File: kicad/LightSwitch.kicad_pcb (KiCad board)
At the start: 2 copper layers, 42 x 70 mm, 26 parts, among them J2 RJ45, J3 RJ45, SW1 Pushbutton_LED, SW2 Pushbutton_LED, SW3 Pushbutton_LED, SW4 Pushbutton_LED, SW5 Pushbutton_LED, SW6 Pushbutton_LED, U1 LM1117-5.0, U2 ATtiny406-M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

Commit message: Parking stuff, so I can contemplate the use of a nrf52840 _with_ DALI
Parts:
- removed J3: RJ45, Connector_RJ:RJ45_Amphenol_54602-x08_Horizontal
- removed PROG: Conn_01x03_Male, Connector_PinHeader_2.54mm:PinHeader_1x03_P2.54mm_Vertical
- removed R3, R8: 220, Resistor_SMD:R_0805_2012Metric
- removed REF** (x4): MountingHole_3mm_Pad, MountingHole:MountingHole_3mm_Pad
- removed SW6: Pushbutton_LED, LightSwitch:12x12x7.3 LED Pushbutton
- removed TERM: Jumper, Connector_PinHeader_2.54mm:PinHeader_1x02_P2.54mm_Vertical
- added C3: 10u, Capacitor_SMD:C_0805_2012Metric, F.Cu at (118.4, 74.6)
- added C4: 0.1u, Capacitor_SMD:C_0805_2012Metric, F.Cu at (121.0, 145.2)
- added C5: 0.1u, Capacitor_SMD:C_0805_2012Metric, F.Cu at (116.2, 99.8)
- added D1: 1N4148WS, Diode_SMD:D_SOD-323, F.Cu at (119.3, 67.5)
- added D2: D_Bridge_+-AA, imported_modules:SOIC245P670X290-4N, F.Cu at (121.1, 43.6)
- added D3: 1N4148WS, Diode_SMD:D_SOD-323, F.Cu at (124.2, 52.3)
- added D4: 1N4148WS, Diode_SMD:D_SOD-323, F.Cu at (127.6, 52.3)
- added J1: Screw_Terminal_01x02, TerminalBlock_Phoenix:TerminalBlock_Phoenix_MKDS-1,5-2-5.08_1x02_P5.08mm_Horizontal, B.Cu at (118.5, 25.4)
- added Q1: MMBT2222A, Package_TO_SOT_SMD:SOT-23, F.Cu at (116.5, 51.5)
- added R1: 4.7K, Resistor_SMD:R_0805_2012Metric, F.Cu at (128.2, 97.0)
- C1: value 0.1u -> 10u
- C2: value 10u -> 0.1u
- J2: value RJ45 -> Conn_01x03_Male; footprint Connector_RJ:RJ45_Amphenol_54602-x08_Horizontal -> Connector_PinHeader_2.54mm:PinHeader_1x03_P2.54mm_Vertical; moved to F.Cu
- R2: value 220 -> 4.7K
- R4: value 220 -> 120
- R5: value 120 -> 1K
- R6: value 220 -> 27K
- R7: value 220 -> 2K
- SW1, SW2, SW3, SW4, SW5: value Pushbutton_LED -> SW_Push; footprint LightSwitch:12x12x7.3 LED Pushbutton -> Button_Switch_THT:SW_PUSH-12mm
- U1: value LM1117-5.0 -> LM2936-3.3; footprint Package_TO_SOT_SMD:SOT-223-3_TabPin2 -> Package_TO_SOT_SMD:SOT-223
- U2: value ATtiny406-M -> SHT35-DIS; footprint Package_DFN_QFN:VQFN-20-1EP_3x3mm_P0.4mm_EP1.7x1.7mm -> Sensor_Humidity:Sensirion_DFN-8-1EP_2.5x2.5mm_P0.5mm_EP1.1x1.7mm
- U3: value SN65HVD232 -> ATtiny804-SS; footprint Package_SO:SOIC-8_3.9x4.9mm_P1.27mm -> Package_SO:SOIC-14_3.9x8.7mm_P1.27mm
- moved R6 108.0 mm to (124.1, 50.2), turned to 0 degrees
- moved R5 100.2 mm to (113.5, 51.5), turned to -90 degrees
- moved R7 99.4 mm to (127.7, 50.2)
- moved SW2 99.1 mm to (115.0, 57.0)
- moved SW4 97.8 mm to (115.0, 107.0)
- moved C1 97.1 mm to (117.2, 71.0)
- moved C2 93.7 mm to (119.3, 71.0), turned to -90 degrees
- moved R4 91.4 mm to (114.5, 48.7), turned to 180 degrees
- moved U2 90.6 mm to (121.0, 142.5), turned to -90 degrees
- moved SW1 84.3 mm to (115.0, 32.0)
- moved U1 83.5 mm to (124.8, 72.2)
- moved J2 81.2 mm to (112.1, 93.6), turned to 90 degrees
- moved U3 79.3 mm to (121.9, 99.5), turned to 90 degrees
- moved SW3 74.5 mm to (115.2, 82.0)
- moved SW5 72.8 mm to (115.0, 132.0)
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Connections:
- C1 pad 1: VDD -> Net-(C1-Pad1)
- C2 pad 1: VDD -> Net-(C1-Pad1)
- J2 pad 1: /CANH -> VDD
- J2 pad 2: /CANL -> /PROG
- R2 pad 1: /LED1 -> VDD
- R2 pad 2: Net-(R2-Pad2) -> /SCL
- R4 pad 1: /LED3 -> Net-(Q1-Pad1)
- R4 pad 2: Net-(R4-Pad2) -> /DALI_TX
- R5 pad 1: Net-(JP1-Pad2) -> /DALI_TX
- R5 pad 2: /CANL -> GND
- R6 pad 1: /LED4 -> /DALI+
- R6 pad 2: Net-(R6-Pad2) -> /DALI_RX
- R7 pad 1: /LED5 -> /DALI_RX
- R7 pad 2: Net-(R7-Pad2) -> GND
- SW1 pad 1: GND -> /SW1
- SW1 pad 2: Net-(SW1-Pad2) -> GND
- SW2 pad 1: GND -> /SW2
- SW2 pad 2: Net-(SW2-Pad2) -> GND
- SW3 pad 1: GND -> /SW3
- SW3 pad 2: Net-(SW3-Pad2) -> GND
- SW4 pad 1: GND -> /SW4
- SW4 pad 2: Net-(SW4-Pad2) -> GND
- SW5 pad 1: GND -> /SW5
- SW5 pad 2: Net-(SW5-Pad2) -> GND
- U1 pad 1: GND -> Net-(C1-Pad1)
- U1 pad 2: VDD -> GND
- U1 pad 3: /VIN -> VDD
- U2 pad 1: Net-(U2-Pad1) -> /SDA
- U2 pad 2: Net-(U2-Pad2) -> GND
- U2 pad 3: GND -> /TEMP_ALERT
- U2 pad 4: VDD -> /SCL
- U2 pad 5: /LED3 -> VDD
- U2 pad 6: /SW3 -> unconnected-(U2-Pad6)
- U2 pad 7: /LED5 -> GND
- U2 pad 8: /SW5 -> GND
- U2 pad 9: /LED6 -> GND
- U3 pad 1: /CAN_TX -> VDD
- U3 pad 2: GND -> /SW4
- U3 pad 3: VDD -> /SW5
- U3 pad 4: /CAN_RX -> /DALI_TX
- U3 pad 5: Net-(U3-Pad5) -> /DALI_RX
- U3 pad 6: /CANL -> /TEMP_ALERT
- U3 pad 7: /CANH -> /SCL
- U3 pad 8: Net-(U3-Pad8) -> /SDA
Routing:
- net VDD: track 40.3 -> 129.6 mm
- net /DALI_TX: track 0.00 -> 68.0 mm
- net /DALI_RX: track 0.00 -> 62.4 mm
- net /SDA: track 0.00 -> 54.8 mm
- net /LED1: track 54.3 -> 0.00 mm
- net /CANL: track 50.8 -> 0.00 mm, vias 1 -> 0
- net /TEMP_ALERT: track 0.00 -> 48.3 mm
- net /SW1: track 43.9 -> 87.5 mm
- net GND: track 18.0 -> 61.2 mm, vias 6 -> 0
- net /SCL: track 0.00 -> 43.1 mm
- net /VIN: track 37.0 -> 0.00 mm
- net Net-(J2-Pad7): track 36.3 -> 0.00 mm
- net /CANH: track 35.6 -> 0.00 mm
- net /LED2: track 34.6 -> 0.00 mm
- net /LED5: track 31.7 -> 0.00 mm
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- added copper zone on F.Cu, net GND
- removed copper zone on B.Cu, net GND
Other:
- board size 42 x 70 mm -> 42 x 129.3 mm
- net class Default removed
- board text added: "GND"
- board text added: "PRG"
- board text added: "VDD"

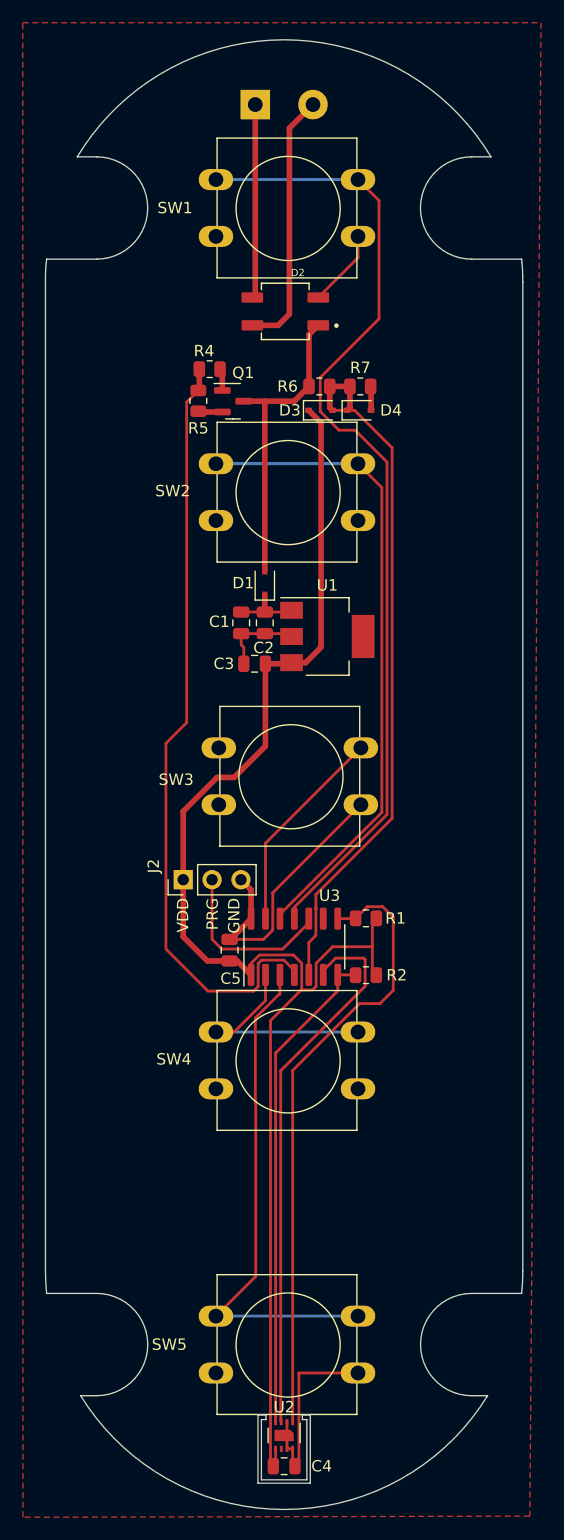
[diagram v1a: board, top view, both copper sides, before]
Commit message: Updated with NRF52840 version. Modded since sending to OSHPark
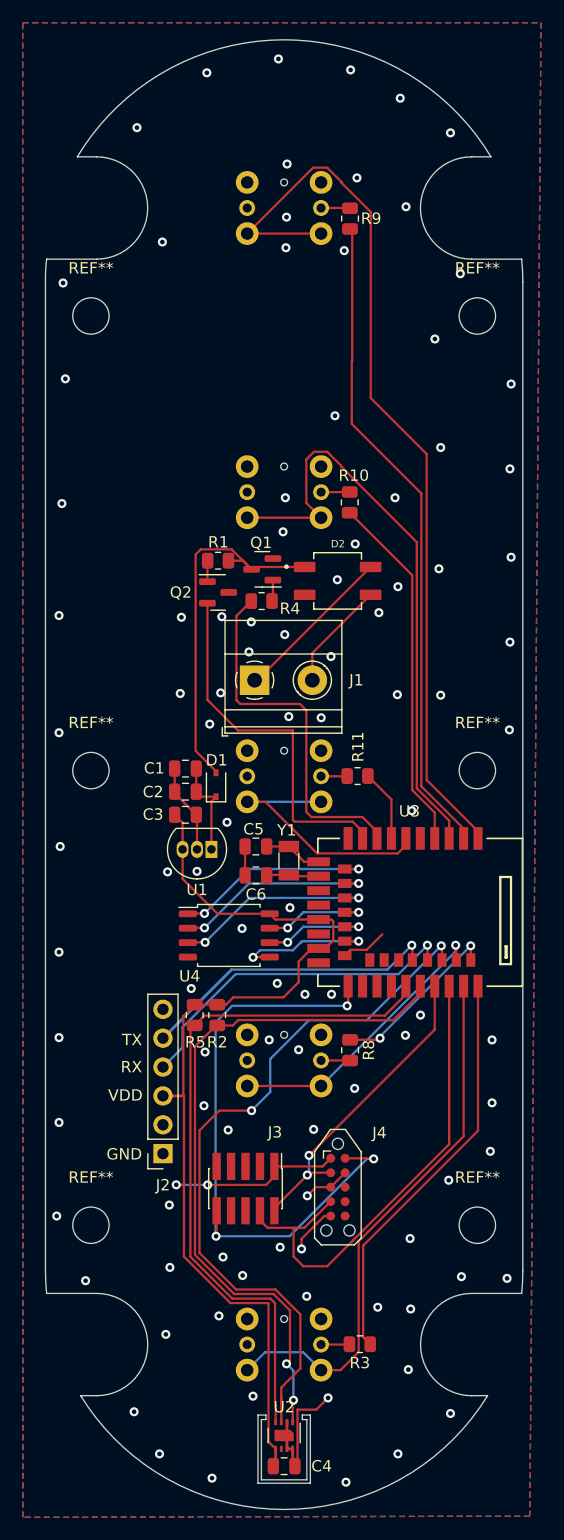
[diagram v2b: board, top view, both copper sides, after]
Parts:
- removed D3, D4: 1N4148WS, Diode_SMD:D_SOD-323
- removed R6: 27K, Resistor_SMD:R_0805_2012Metric
- removed R7: 2K, Resistor_SMD:R_0805_2012Metric
- added C6: 12pf, Capacitor_SMD:C_0805_2012Metric, F.Cu at (118.5, 93.2)
- added J3: Conn_ARM_JTAG_SWD_10, Connector_PinHeader_1.27mm:PinHeader_2x05_P1.27mm_Vertical_SMD, F.Cu at (117.6, 120.8)
- added J4: Conn_ARM_JTAG_SWD_10, Connector:Tag-Connect_TC2050-IDC-NL_2x05_P1.27mm_Vertical, F.Cu at (125.7, 120.7)
- added Q2: MMBT2222A, Package_TO_SOT_SMD:SOT-23, F.Cu at (115.2, 68.3)
- added R10: 330, Resistor_SMD:R_0805_2012Metric, F.Cu at (126.8, 60.4)
- added R11: 330, Resistor_SMD:R_0805_2012Metric, F.Cu at (127.5, 84.5)
- added R3: 330, Resistor_SMD:R_0805_2012Metric, F.Cu at (127.7, 134.5)
- added R8: 330, Resistor_SMD:R_0805_2012Metric, F.Cu at (126.8, 108.6)
- added R9: 330, Resistor_SMD:R_0805_2012Metric, F.Cu at (126.8, 35.4)
- added REF**: MountingHole_3.2mm_M3, MountingHole:MountingHole_3.2mm_M3, F.Cu at (104.0, 84.0)
- added REF**: MountingHole_3.2mm_M3, MountingHole:MountingHole_3.2mm_M3, F.Cu at (138.0, 84.0)
- added REF**: MountingHole_3.2mm_M3, MountingHole:MountingHole_3.2mm_M3, F.Cu at (104.0, 44.0)
- added REF**: MountingHole_3.2mm_M3, MountingHole:MountingHole_3.2mm_M3, F.Cu at (104.0, 124.0)
- added REF**: MountingHole_3.2mm_M3, MountingHole:MountingHole_3.2mm_M3, F.Cu at (138.0, 44.0)
- added REF**: MountingHole_3.2mm_M3, MountingHole:MountingHole_3.2mm_M3, F.Cu at (138.0, 124.0)
- added U4: MX25R3235FM2xx0, Package_SO:SOP-8_5.28x5.23mm_P1.27mm, F.Cu at (116.1, 98.5)
- added Y1: 32.768kHz, Crystal:Crystal_SMD_3215-2Pin_3.2x1.5mm, F.Cu at (121.4, 91.9)
- C5: value 0.1u -> 12pf
- J1: moved to F.Cu
- J2: value Conn_01x03_Male -> Conn_01x06_Female; footprint Connector_PinHeader_2.54mm:PinHeader_1x03_P2.54mm_Vertical -> Connector_PinSocket_2.54mm:PinSocket_1x06_P2.54mm_Vertical
- R1: value 4.7K -> 2.2K
- R2: value 4.7K -> 10K
- R5: value 1K -> 10K
- SW1, SW2, SW3, SW4, SW5: value SW_Push -> SW_Push_LED; footprint Button_Switch_THT:SW_PUSH-12mm -> LocalProject:LED Pushbutton; moved to B.Cu
- U1: value LM2936-3.3 -> LM2936-3.0; footprint Package_TO_SOT_SMD:SOT-223 -> Package_TO_SOT_THT:TO-92_Inline
- U3: value ATtiny804-SS -> E73-2G4M08S1C; footprint Package_SO:SOIC-14_3.9x8.7mm_P1.27mm -> E73-2G4M08S1C:E73-2G4M08S1C
- moved R5 54.0 mm to (113.1, 105.5)
- moved J1 50.6 mm to (118.4, 76.0)
- moved R1 34.1 mm to (115.2, 65.5)
- moved J2 24.2 mm to (110.3, 117.7), turned to 180 degrees
- moved D2 24.2 mm to (125.7, 67.3), turned to 0 degrees
- moved U1 21.3 mm to (114.6, 90.9), turned to 180 degrees
- moved R4 20.9 mm to (119.0, 69.1)
- moved D1 18.3 mm to (115.0, 85.2)
- moved C2 16.4 mm to (112.3, 85.9), turned to 180 degrees
- moved Q1 15.0 mm to (119.1, 66.3), turned to 180 degrees
- moved C3 14.6 mm to (112.3, 87.9), turned to 0 degrees
- moved C1 13.7 mm to (112.3, 83.8), turned to 180 degrees
- moved R2 13.6 mm to (115.1, 105.5), turned to -90 degrees
- moved U3 9.63 mm to (131.0, 96.5)
- moved C5 9.41 mm to (118.5, 90.7), turned to 180 degrees
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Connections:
- C5 pad 1: GND -> Net-(C5-Pad1)
- C5 pad 2: VDD -> GND
- J1 pad 1: /D1 -> /D2
- J1 pad 2: /D2 -> /D1
- J2 pad 1: VDD -> GND
- J2 pad 2: /PROG -> unconnected-(J2-Pad2)
- J2 pad 3: GND -> VDD
- R1 pad 1: VDD -> /DALI+
- R1 pad 2: /SDA -> Net-(Q2-Pad1)
- R2 pad 2: /SCL -> /SDA
- R5 pad 1: /DALI_TX -> VDD
- R5 pad 2: GND -> /SCL
- SW1 pad 1: /SW1 -> GND
- SW1 pad 2: GND -> /SW1
- SW2 pad 1: /SW2 -> GND
- SW2 pad 2: GND -> /SW2
- SW3 pad 1: /SW3 -> GND
- SW3 pad 2: GND -> /SW3
- SW4 pad 1: /SW4 -> GND
- SW4 pad 2: GND -> /SW4
- SW5 pad 1: /SW5 -> GND
- SW5 pad 2: GND -> /SW5
- U3 pad 1: VDD -> /SW1
- U3 pad 10: /PROG -> unconnected-(U3-Pad10)
- U3 pad 11: /SW1 -> Net-(C5-Pad1)
- U3 pad 12: /SW2 -> /CS
- U3 pad 13: /SW3 -> Net-(C6-Pad1)
- U3 pad 14: GND -> /SIO_1
- U3 pad 2: /SW4 -> /LED1
- U3 pad 3: /SW5 -> /SW2
- U3 pad 4: /DALI_TX -> /LED2
- U3 pad 5: /DALI_RX -> GND
- U3 pad 6: /TEMP_ALERT -> /SW3
- U3 pad 7: /SCL -> /LED3
- U3 pad 8: /SDA -> /DALI_TX
- U3 pad 9: unconnected-(U3-Pad9) -> /DALI_RX
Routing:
- net /LED1: track 0.00 -> 57.8 mm
- net /~{RESET}: track 0.00 -> 54.3 mm, vias 0 -> 3
- net /SWDCLK: track 0.00 -> 43.3 mm
- net /LED5: track 0.00 -> 35.9 mm
- net /DALI_TX: track 68.0 -> 32.3 mm
- net /LED2: track 0.00 -> 31.8 mm
- net /DALI_RX: track 62.4 -> 32.2 mm
- net /RX: track 0.00 -> 30.1 mm, vias 0 -> 1
- net VDD: track 129.6 -> 101.4 mm, vias 0 -> 2
- net /SWDIO: track 0.00 -> 27.7 mm, vias 0 -> 2
- net /TX: track 0.00 -> 26.6 mm, vias 0 -> 1
- net GND: track 61.2 -> 35.8 mm, vias 0 -> 101
- net /SIO_1: track 0.00 -> 17.9 mm, vias 0 -> 2
- net /SIO_2: track 0.00 -> 17.9 mm, vias 0 -> 2
- net /CS: track 0.00 -> 17.9 mm, vias 0 -> 2
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- added copper zone on B.Cu, net GND
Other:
- board text added: "RX"
- board text added: "TX"
- board text removed: "PRG"
